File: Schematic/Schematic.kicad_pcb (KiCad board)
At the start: 2 copper layers, 67.5 x 55 mm, 17 parts, among them J3 FTDI, SW1 SW_Push, U1 ATmega328P-A, Y1 16 Mhz

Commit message: error PCB done 12 warning to do
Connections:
- C3 pad 1: Net-(#PWR12-Pad1) -> VCC
- C4 pad 1: Net-(#PWR10-Pad1) -> GND
- C6 pad 2: Net-(#PWR1-Pad1) -> GND
- C7 pad 2: Net-(#PWR4-Pad1) -> GND
- D1 pad 2: Net-(#PWR9-Pad1) -> GND
- R2 pad 2: Net-(#PWR6-Pad1) -> GND
- R3 pad 1: Net-(#PWR11-Pad1) -> VCC
- U1 pad 18: Net-(U1-AVCC) -> VCC
- U1 pad 3: Net-(U1-GND) -> GND
- U1 pad 31: RXO -> TXO
- U1 pad 4: Net-(U1-AVCC) -> VCC
- Y1 pad 2: Net-(#PWR8-Pad1) -> GND
- Y1 pad 4: Net-(#PWR7-Pad1) -> GND
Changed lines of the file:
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@@
 	(net 32 "A7")
 	(net 33 "A4")
-	(net 34 "Net-(#PWR12-Pad1)")
-	(net 35 "Net-(#PWR10-Pad1)")
-	(net 36 "Net-(#PWR1-Pad1)")
-	(net 37 "Net-(#PWR4-Pad1)")
-	(net 38 "Net-(#PWR9-Pad1)")
-	(net 39 "Net-(#PWR6-Pad1)")
-	(net 40 "Net-(#PWR11-Pad1)")
-	(net 41 "Net-(U1-GND)")
-	(net 42 "RXO")
-	(net 43 "Net-(U1-AVCC)")
-	(net 44 "Net-(#PWR7-Pad1)")
 	(footprint "Library:SMD_603"
 		(layer "F.Cu")
@@
 			(layers "F.Cu")
 			(roundrect_rratio 0.1968503937)
-			(net 40 "Net-(#PWR11-Pad1)")
+			(net 24 "VCC")
 			(pintype "passive")
 		)
@@
 			(layers "F.Cu" "F.Paste")
 			(roundrect_rratio 0.1968503937)
-			(net 36 "Net-(#PWR1-Pad1)")
+			(net 17 "GND")
 			(pintype "passive")
 		)
@@
 			(size 0.55 1.55)
 			(layers "F.Cu")
-			(net 41 "Net-(U1-GND)")
+			(net 17 "GND")
 			(pinfunction "GND")
 			(pintype "power_in")
@@
 			(size 0.55 1.55)
 			(layers "F.Cu")
-			(net 43 "Net-(U1-AVCC)")
+			(net 24 "VCC")
 			(pinfunction "VCC")
 			(pintype "power_in")
@@
 			(size 0.55 1.55)
 			(layers "F.Cu")
-			(net 43 "Net-(U1-AVCC)")
+			(net 24 "VCC")
 			(pinfunction "AVCC")
 			(pintype "power_in")
@@
 			(size 0.55 1.55)
 			(layers "F.Cu")
-			(net 42 "RXO")
+			(net 9 "TXO")
 			(pinfunction "PD1")
 			(pintype "bidirectional")
@@
 			(layers "F.Cu" "F.Paste")
 			(roundrect_rratio 0.1968503937)
-			(net 34 "Net-(#PWR12-Pad1)")
+			(net 24 "VCC")
 			(pintype "passive")
 		)
@@
 			(layers "F.Cu")
 			(roundrect_rratio 0.1968503937)
-			(net 35 "Net-(#PWR10-Pad1)")
+			(net 17 "GND")
 			(pintype "passive")
 		)
@@
 			(layers "F.Cu" "F.Paste")
 			(roundrect_rratio 0.1968503937)
-			(net 37 "Net-(#PWR4-Pad1)")
+			(net 17 "GND")
 			(pintype "passive")
 		)
@@
 			(layers "F.Cu")
 			(roundrect_rratio 0.1968503937)
-			(net 38 "Net-(#PWR9-Pad1)")
+			(net 17 "GND")
 			(pintype "passive")
 		)
@@
 			(layers "F.Cu" "F.Mask" "F.Paste")
 			(roundrect_rratio 0.15)
-			(net 2 "Net-(#PWR8-Pad1)")
+			(net 17 "GND")
 			(pintype "power_in")
 		)
@@
 			(layers "F.Cu" "F.Mask" "F.Paste")
 			(roundrect_rratio 0.15)
-			(net 44 "Net-(#PWR7-Pad1)")
+			(net 17 "GND")
 			(pintype "power_in")
 		)
@@
 			(layers "F.Cu")
 			(roundrect_rratio 0.1968503937)
-			(net 39 "Net-(#PWR6-Pad1)")
-			(pintype "passive")
-		)
+			(net 17 "GND")
+			(pintype "passive")
+		)

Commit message: warnings still to do
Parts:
- C1, C2, C3, C4, C6, C7, D1, D2, R1, R2, R3: footprint Library:SMD_603 -> Library:SmD_603
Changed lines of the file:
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@@
 	(net 32 "A7")
 	(net 33 "A4")
-	(footprint "Library:SMD_603"
+	(footprint "Library:SmD_603"
 		(layer "F.Cu")
 		(at 146.6 122.5)
@@
 		(embedded_fonts no)
 	)
-	(footprint "Library:SMD_603"
+	(footprint "Library:SmD_603"
 		(layer "F.Cu")
 		(at 136.5 121.5)
@@
 			)
 		)
-		(property "Datasheet" "https://yageogroup.com/content/datasheet/asset/file/UPY-GPHC_X7R_6_3V-TO-250V"
+		(property "Datasheet" "https://yageogroup.com/content/datasheet/asset/file/PYU-RC_GROUP_51_ROHS_L"
 			(at 0 0 0)
 			(unlocked yes)
@@
 			(at -0.9 0)
 			(size 0.95 1.08)
-			(layers "F.Cu" "F.Paste")
+			(layers "F.Cu")
 			(roundrect_rratio 0.1968503937)
 			(net 3 "Net-(U1-XTAL1{slash}PB6)")
@@
 			(at 0.9 0)
 			(size 0.95 1.08)
-			(layers "F.Cu" "F.Paste")
+			(layers "F.Cu")
 			(roundrect_rratio 0.1968503937)
 			(net 2 "Net-(#PWR8-Pad1)")
@@
 		(embedded_fonts no)
 	)
-	(footprint "Library:SMD_603"
+	(footprint "Library:SmD_603"
 		(layer "F.Cu")
 		(at 145.1 108.5 180)
@@
 			)
 		)
-		(property "Datasheet" "https://yageogroup.com/content/datasheet/asset/file/UPY-GPHC_X7R_6_3V-TO-250V"
+		(property "Datasheet" "https://yageogroup.com/content/datasheet/asset/file/PYU-RC_GROUP_51_ROHS_L"
 			(at 0 0 180)
 			(unlocked yes)
@@
 			(at -0.9 0 180)
 			(size 0.95 1.08)
-			(layers "F.Cu" "F.Paste")
+			(layers "F.Cu")
 			(roundrect_rratio 0.1968503937)
 			(net 6 "RAW")
@@
 			(at 0.9 0 180)
 			(size 0.95 1.08)
-			(layers "F.Cu" "F.Paste")
+			(layers "F.Cu")
 			(roundrect_rratio 0.1968503937)
 			(net 17 "GND")
 			(pintype "passive")
+			(teardrops
+				(best_length_ratio 0.5)
+				(max_length 1)
+				(best_width_ratio 1)
+				(max_width 2)
+				(curved_edges no)
+				(filter_ratio 0.9)
+				(enabled yes)
+				(allow_two_segments yes)
+				(prefer_zone_connections yes)
+			)
 		)
 		(embedded_fonts no)
@@
 		(embedded_fonts no)
 	)
-	(footprint "Library:SMD_603"
+	(footprint "Library:SmD_603"
 		(layer "F.Cu")
 		(at 168.5 116.6 -90)
@@
 			)
 		)
-		(property "Datasheet" "https://yageogroup.com/content/datasheet/asset/file/UPY-GPHC_X7R_6_3V-TO-250V"
+		(property "Datasheet" "https://yageogroup.com/content/datasheet/asset/file/PYU-RC_GROUP_51_ROHS_L"
 			(at 0 0 270)
 			(unlocked yes)
@@
 			(at -0.9 0 270)
 			(size 0.95 1.08)
-			(layers "F.Cu" "F.Paste")
+			(layers "F.Cu")
 			(roundrect_rratio 0.1968503937)
 			(net 24 "VCC")
@@
 			(at 0.9 0 270)
 			(size 0.95 1.08)
-			(layers "F.Cu" "F.Paste")
+			(layers "F.Cu")
 			(roundrect_rratio 0.1968503937)
 			(net 4 "Net-(U1-AREF)")
@@
 		(embedded_fonts no)
 	)
-	(footprint "Library:SMD_603"
+	(footprint "Library:SmD_603"
 		(layer "F.Cu")
 		(at 163 116.6 -90)
@@
 		(embedded_fonts no)
 	)
-	(footprint "Library:SMD_603"
+	(footprint "Library:SmD_603"
 		(layer "F.Cu")
 		(at 147 139.5 90)
@@
 			)
 		)
-		(property "Datasheet" "https://yageogroup.com/content/datasheet/asset/file/UPY-GPHC_X7R_6_3V-TO-250V"
+		(property "Datasheet" "https://yageogroup.com/content/datasheet/asset/file/PYU-RC_GROUP_51_ROHS_L"
 			(at 0 0 90)
 			(unlocked yes)
@@
 		(embedded_fonts no)
 	)
-	(footprint "Library:SMD_603"
+	(footprint "Library:SmD_603"
 		(layer "F.Cu")
 		(at 132.5 106.9 -90)
@@
 			)
 		)
-		(property "Datasheet" "https://yageogroup.com/content/datasheet/asset/file/UPY-GPHC_X7R_6_3V-TO-250V"
+		(property "Datasheet" "https://yageogroup.com/content/datasheet/asset/file/PYU-RC_GROUP_51_ROHS_L"
 			(at 0 0 270)
 			(unlocked yes)
@@
 			(at -0.9 0 270)
 			(size 0.95 1.08)
-			(layers "F.Cu" "F.Paste")
+			(layers "F.Cu")
 			(roundrect_rratio 0.1968503937)
 			(net 6 "RAW")
@@
 			(at 0.9 0 270)
 			(size 0.95 1.08)
-			(layers "F.Cu" "F.Paste")
+			(layers "F.Cu")
 			(roundrect_rratio 0.1968503937)
 			(net 17 "GND")
@@
 		(embedded_fonts no)
 	)
-	(footprint "Library:SMD_603"
+	(footprint "Library:SmD_603"
 		(layer "F.Cu")
 		(at 147 114.6 -90)
@@
 			)
 		)
-		(property "Datasheet" "https://yageogroup.com/content/datasheet/asset/file/UPY-GPHC_X7R_6_3V-TO-250V"
+		(property "Datasheet" "https://yageogroup.com/content/datasheet/asset/file/PYU-RC_GROUP_51_ROHS_L"
 			(at 0 0 270)
 			(unlocked yes)
@@
 			(at -0.9 0 270)
 			(size 0.95 1.08)
-			(layers "F.Cu" "F.Paste")
+			(layers "F.Cu")
 			(roundrect_rratio 0.1968503937)
 			(net 1 "Net-(U1-XTAL2{slash}PB7)")
@@
 			(at 0.9 0 270)
 			(size 0.95 1.08)
-			(layers "F.Cu" "F.Paste")
+			(layers "F.Cu")
 			(roundrect_rratio 0.1968503937)
 			(net 2 "Net-(#PWR8-Pad1)")
@@
 		(embedded_fonts no)
 	)
-	(footprint "Library:SMD_603"
+	(footprint "Library:SmD_603"
 		(layer "F.Cu")
 		(at 158 116.5 90)
@@
 			)
 		)
-		(property "Datasheet" "https://cdn-reichelt.de/documents/datenblatt/A500/KP-1608ID(VER.9A).pdf"
+		(property "Datasheet" "https://yageogroup.com/content/datasheet/asset/file/PYU-RC_GROUP_51_ROHS_L"
 			(at 0 0 90)
 			(unlocked yes)
@@
 		(embedded_fonts no)
 	)
-	(footprint "Library:SMD_603"
+	(footprint "Library:SmD_603"
 		(layer "F.Cu")
 		(at 145.03 104.53 180)
@@
 			)
 		)
-		(property "Datasheet" "https://cdn-reichelt.de/documents/datenblatt/A500/KP-1608ID(VER.9A).pdf"
+		(property "Datasheet" "https://yageogroup.com/content/datasheet/asset/file/PYU-RC_GROUP_51_ROHS_L"
 			(at 0 0 180)
 			(unlocked yes)
@@
 		(at 136.9 114.6)
 		(property "Reference" "Y1"
-			(at -1.7 -2.2 0)
+			(at -0.9 -2.2 0)
 			(unlocked yes)
 			(layer "F.SilkS")
 			(effects
 				(font
-					(size 0.5 0.5)
+					(size 0.8 0.8)
 					(thickness 0.1)
 				)
@@
 		)
 		(property "Value" "16 Mhz"
-			(at 0.6 -2.2 0)
+			(at 2.6 -2.2 0)
 			(unlocked yes)
 			(layer "F.SilkS")
 			(effects
 				(font
-					(size 0.5 0.5)
+					(size 0.8 0.8)
 					(thickness 0.1)
 					(bold yes)
@@
 			(layer "F.CrtYd")
 		)
-		(fp_text user "GND"
-			(at -3.9 -0.5 0)
+		(fp_text user "G"
+			(at -3.4 -0.6 0)
 			(unlocked yes)
 			(layer "F.SilkS")
 			(effects
 				(font
-					(size 0.5 0.5)
+					(size 0.8 0.8)
 					(thickness 0.1)
 				)
@@
 		)
 		(fp_text user "GND"
-			(at 2.3 2.4 0)
+			(at 2.3 2.9 0)
 			(unlocked yes)
 			(layer "F.SilkS")
 			(effects
 				(font
-					(size 0.5 0.5)
+					(size 0.8 0.8)
 					(thickness 0.1)
 				)
@@
 		(embedded_fonts no)
 	)
-	(footprint "Library:SMD_603"
+	(footprint "Library:SmD_603"
 		(layer "F.Cu")
 		(at 139.35 106 180)
@@
 		(net 29)
 	)
+	(zone
+		(net 17)
+		(net_name "GND")
+		(layer "F.Cu")
+		(name "$teardrop_padvia$")
+		(hatch none 0.1)
+		(priority 30000)
+		(attr
+			(teardrop
+				(type padvia)
+			)
+		)
+		(connect_pads yes
+			(clearance 0)
+		)
+		(min_thickness 0.0254)
+		(filled_areas_thickness no)
+		(fill yes
+			(thermal_gap 0.5)
+			(thermal_bridge_width 0.5)
+			(island_removal_mode 1)
+			(island_area_min 10)
+		)
+		(polygon
+			(pts
+				(xy 143.25 108.4) (xy 143.25 108.6) (xy 143.77294 108.975) (xy 144.201 108.5) (xy 143.77294 108.025)
+			)
+		)
+	)
 	(embedded_fonts no)

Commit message: pcb working
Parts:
- C1, C2, C3, C4, C6, C7, D1, D2, R1, R2, R3: footprint Library:SmD_603 -> Library:SMD_603
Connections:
- C1 pad 2: Net-(#PWR8-Pad1) -> GND
- C2 pad 2: Net-(#PWR8-Pad1) -> GND
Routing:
- net Net-(#PWR8-Pad1): track 53.8 -> 0.00 mm
- net GND: track 280.1 -> 320.4 mm
- net VCC: track 163.0 -> 131.1 mm
- net A1: track 61.1 -> 31.0 mm
- net Net-(U1-XTAL1/PB6): track 117.2 -> 108.4 mm
- net Net-(U1-XTAL2/PB7): track 113.0 -> 110.8 mm
- net SCK: track 36.6 -> 37.3 mm
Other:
- board text added: "C3"
- board text added: "C7"
- board text added: "D2"
- board text added: "R2"
- board text added: "R3"

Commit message: finished
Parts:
- removed SW1: SW_Push, Library:Interrupter_SMD_Omron_B3S-1000
- added REF**: interupter_SMD_B3U-1000P(M), Library:interupter_SMD_B3U-1000P(M), F.Cu at (149.0, 127.5)
- moved C7 32.2 mm to (159.5, 124.5)
- moved C6 19.9 mm to (157.0, 124.5), turned to -90 degrees
- moved C4 12.6 mm to (143.0, 127.5), turned to 0 degrees
- moved D2 7.93 mm to (150.9, 109.9)
- moved R2 7.85 mm to (146.1, 110.0)
- moved C1 6.00 mm to (141.0, 114.5)
- moved C2 2.65 mm to (136.0, 118.9), turned to -90 degrees
- moved R1 1.50 mm to (164.5, 116.6)
- moved D1 1.00 mm to (159.0, 116.5), turned to -90 degrees
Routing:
- net GND: track 320.4 -> 197.7 mm, vias 5 -> 6
- net TXO: track 176.0 -> 128.8 mm
- net Net-(U1-XTAL1/PB6): track 108.4 -> 67.9 mm
- net RXI: track 131.7 -> 97.8 mm
- net Net-(U1-XTAL2/PB7): track 110.8 -> 84.7 mm
- net DTR: track 156.7 -> 137.4 mm
- net RAW: track 42.0 -> 32.3 mm
- net Net-(C4-Pad2): track 16.1 -> 9.00 mm
- net A3: track 28.5 -> 23.0 mm
- net A1: track 31.0 -> 34.6 mm
- net D4: track 13.5 -> 16.8 mm
- net A0: track 22.6 -> 25.0 mm
- net D3: track 11.9 -> 14.0 mm
- net A2: track 24.9 -> 23.0 mm
- net Net-(D1-Pad1): track 5.03 -> 6.76 mm
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- added copper zone on B.Cu, net GND
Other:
- board size 67.5 x 55 mm -> 58 x 43.5 mm
- board text added: "C1"
- board text added: "C2"
- board text added: "C4"
- board text added: "C6"
- board text added: "D1"
- board text added: "NR"
- board text added: "R1"

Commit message: updated board
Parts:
- C1: footprint Library:SMD_603 -> Library:SMD_603_C1
- C2: footprint Library:SMD_603 -> Library:SMD_603_C2
- C3: footprint Library:SMD_603 -> Library:SMD_603_C3
- C4: footprint Library:SMD_603 -> Library:SMD_603_C4
- D1: footprint Library:SMD_603 -> Library:SMD603_D1
- D2: footprint Library:SMD_603 -> Library:SMD_603_D2
- R1: footprint Library:SMD_603 -> Library:SMD_603_R1
- R2: footprint Library:SMD_603 -> Library:SMD_603_R2
- R3: footprint Library:SMD_603 -> Library:SMD_603_R3
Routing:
- net Net-(D2-Pad2): track 3.55 -> 2.87 mm
- net VCC: track 130.6 -> 130.1 mm
- net Net-(D1-Pad1): track 6.76 -> 6.19 mm
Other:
- board size 58 x 43.5 mm -> 58 x 44.5 mm
- board text added: "+"
- board text removed: "D1"
- board text removed: "NR"

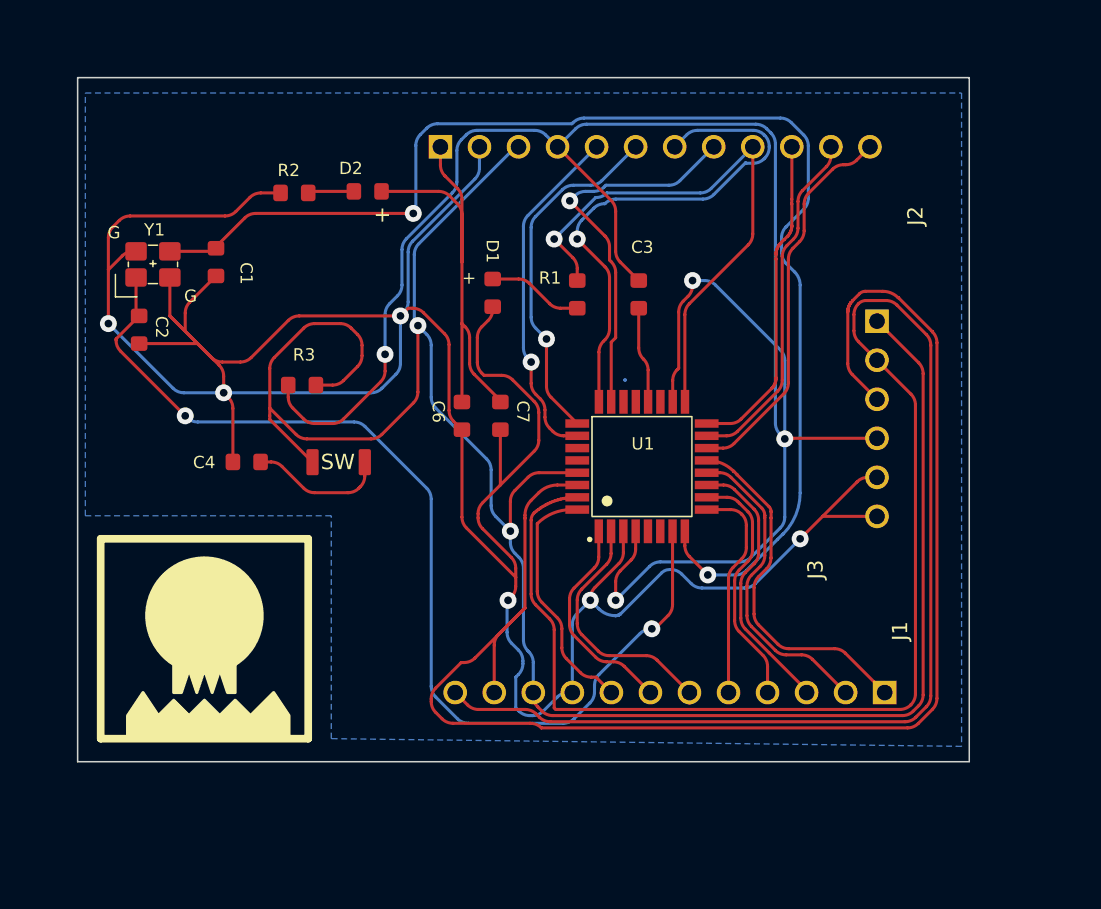
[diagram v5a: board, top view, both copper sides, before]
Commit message: updated silk screen
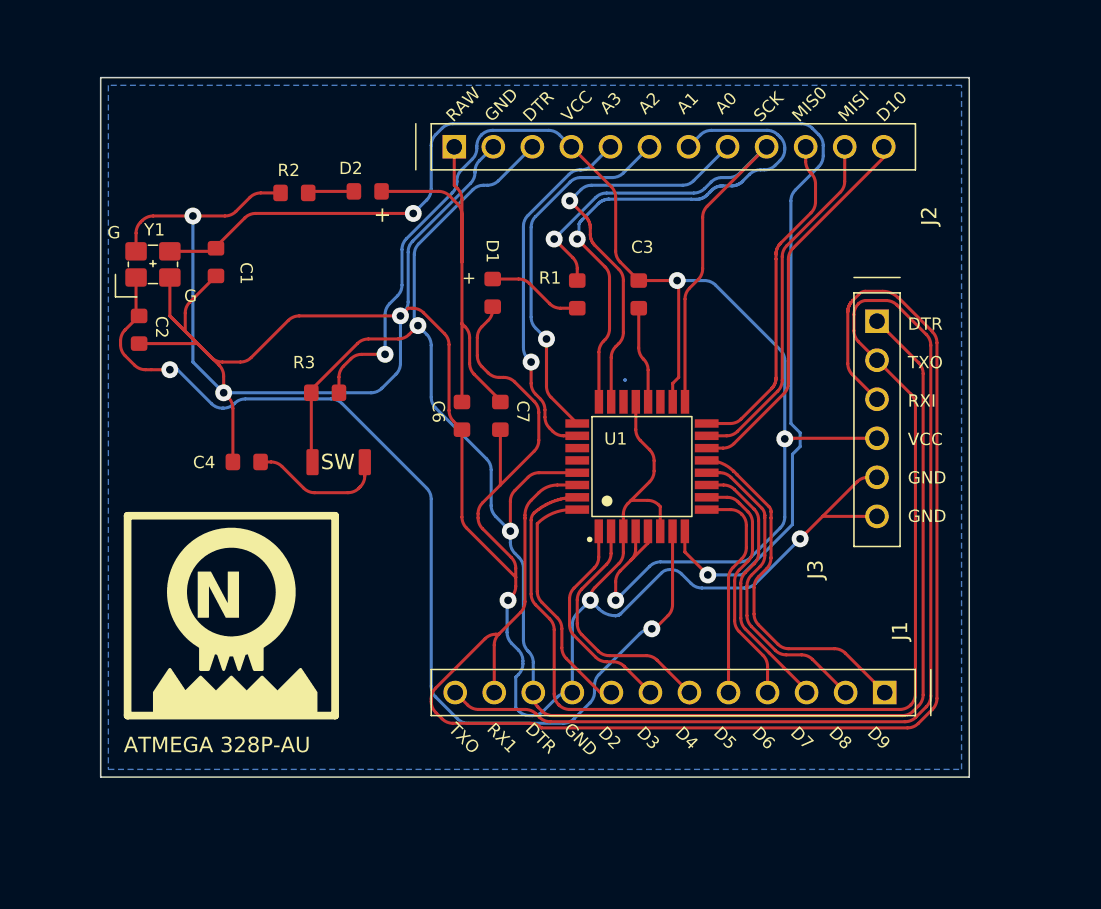
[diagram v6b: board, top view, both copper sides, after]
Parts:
- C6: footprint Library:SMD_603 -> Library:SMD_603_C6
- C7: footprint Library:SMD_603 -> Library:SMD_603_C7
- moved R3 1.58 mm to (148.1, 123.0), turned to 180 degrees
- moved J2 0.90 mm to (170.5, 107.0)
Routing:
- net VCC: track 130.1 -> 95.2 mm
- net DTR: track 137.4 -> 115.4 mm
- net GND: track 197.4 -> 205.2 mm
- net RXI: track 97.8 -> 95.4 mm
- net A0: track 25.0 -> 26.2 mm
- net A1: track 34.3 -> 35.4 mm
- net SCK: track 37.0 -> 38.1 mm
- net A2: track 23.0 -> 23.9 mm
- net A3: track 22.7 -> 23.5 mm
- net MISO: track 21.3 -> 21.9 mm
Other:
- board size 58 x 44.5 mm -> 56.5 x 45.5 mm
- board text added: "A0"
- board text added: "A1"
- board text added: "A2"
- board text added: "A3"
- board text added: "ATMEGA 328P-AU"
- board text added: "D10"
- board text added: "D3"
- board text added: "D4"
- board text added: "D5"
- board text added: "D6"
- board text added: "D7"
- board text added: "D8"
- board text added: "D9"
- board text added: "DTR"
- board text added: "GND"
- board text added: "MIS0"
- board text added: "MISI"
- board text added: "N"
- board text added: "RAW"
- board text added: "RX1"
- board text added: "RXI"
- board text added: "SCK"
- board text added: "TXO"
- board text added: "VCC"
- board text added: "Version 1 - 42-CHIPS - BOOTCAMP - 2026"
